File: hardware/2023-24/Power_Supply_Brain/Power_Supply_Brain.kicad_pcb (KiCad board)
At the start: 4 copper layers, 59 x 84 mm, 99 parts, among them J1 Conn_02x03_Odd_Even, J2 Conn_02x02_Counter_Clockwise, J3 USB_B_Micro, J4 Conn_01x02, J5 Screw_Terminal_01x06, J6 Conn_02x11_Counter_Clockwise, SW1 SW_MEC_5G, U1 MAX17502G, U2 RP2040, U3 NCP1117-3.3_SOT223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

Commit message: design updated post review
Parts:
- removed C24: 24n, Capacitor_SMD:C_0805_2012Metric
- removed R29: 120, Resistor_SMD:R_0603_1608Metric
- removed R30: 3.12k, Resistor_SMD:R_0603_1608Metric
- added C30: 12p, Capacitor_SMD:C_0402_1005Metric, F.Cu at (148.8, 65.5)
- added C31: 2200p, Capacitor_SMD:C_0402_1005Metric, F.Cu at (147.6, 66.9)
- added C32: 22p, Capacitor_SMD:C_0402_1005Metric, F.Cu at (133.5, 93.7)
- added C33: 22u, Capacitor_SMD:C_0805_2012Metric, F.Cu at (128.7, 97.5)
- added R21: 20k, Resistor_SMD:R_0402_1005Metric, F.Cu at (149.2, 67.3)
- added R32: 62k, Resistor_SMD:R_0402_1005Metric, F.Cu at (135.3, 91.0)
- added R33: 30k, Resistor_SMD:R_0402_1005Metric, F.Cu at (135.3, 93.7)
- added R34: 135k, Resistor_SMD:R_0402_1005Metric, F.Cu at (132.3, 93.7)
- added R35: 30k, Resistor_SMD:R_0402_1005Metric, F.Cu at (132.3, 91.0)
- C12: value 2.2u -> 10u
- C16: value 910p -> 6800p
- C18: value 10u -> 100n; footprint Capacitor_SMD:C_0805_2012Metric -> Capacitor_SMD:C_0402_1005Metric
- C20, C21: value 27p -> 15p
- L1: value 39u -> 47u
- R13: value 100k -> 174k
- R16: value 11.1k -> 14k
- R4, R5: value 27 -> 27.4
- U3: value NCP1117-3.3_SOT223 -> TPSM861252RDXR; footprint Package_TO_SOT_SMD:SOT-223-3_TabPin2 -> TPSM861252:RDX0007A-MFG
- U5: value NCP1117-ADJ_SOT223 -> NCP1117-5.0_SOT223
- moved C18 9.26 mm to (128.9, 89.2), turned to 180 degrees
- moved C17 4.21 mm to (128.7, 87.2)
- moved U3 2.60 mm to (128.4, 93.1), turned to -90 degrees
- moved C15 1.30 mm to (132.9, 84.2)
- moved R18 0.85 mm to (122.8, 88.4), turned to 90 degrees
- moved C16 0.78 mm to (150.0, 65.5)
- moved C5 0.70 mm to (147.2, 117.3)
- moved U5 0.10 mm to (153.0, 92.1)
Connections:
- net +5.5V renamed +5V
- net /+9V_LX renamed /+12V_LX
- C18 pad 1: +3V3 -> +9V
- U1 pad 7: unconnected-(U1-NC/COMP-Pad7) -> Net-(U1-NC/COMP)
- U2 pad 11: PGD_B2 -> EN_B3
- U2 pad 12: EN_B2 -> PGD_B2
- U2 pad 13: PGD_B1 -> EN_B2
- U2 pad 14: EN_B1 -> PGD_B1
- U2 pad 15: ALRT_B1 -> EN_B1
- U2 pad 16: ALRT_B2 -> ALRT_B1
- U2 pad 17: ALRT_B3 -> ALRT_B2
- U2 pad 18: unconnected-(U2-GPIO15-Pad18) -> ALRT_B3
- U2 pad 8: PGD_B3 -> LED_EN
- U2 pad 9: EN_B3 -> PGD_B3
- U3 pad 1: GND -> +9V
- U3 pad 2: +3V3 -> unconnected-(U3-SW-Pad2)
- U3 pad 3: +9V -> +3V3
- U5 pad 1: Net-(U5-ADJ) -> GND
- U6 pad 1: +3V3 -> LED_EN
- Y1 pad 2: Net-(C21-Pad1) -> GND
- Y1 pad 3: (no net) -> Net-(C21-Pad1)
- Y1 pad 4: (no net) -> GND
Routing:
- net LED_EN: track 0.00 -> 14.4 mm, vias 0 -> 2
- net Net-(U5-ADJ): track 8.00 -> 0.00 mm
- net Net-(U3-EN): track 0.00 -> 7.04 mm, vias 0 -> 2
- net Net-(U3-FB): track 0.00 -> 4.84 mm
- net GND: track 78.4 -> 82.0 mm, vias 58 -> 57
- net EN_B3: track 35.2 -> 32.1 mm
- net +5V: track 33.4 -> 30.4 mm
- net Net-(U1-NC/COMP): track 0.00 -> 2.87 mm
- net +3V3: track 255.8 -> 258.2 mm, vias 29 -> 19
- net Net-(C21-Pad1): track 7.20 -> 5.50 mm
- net PGD_B3: track 36.6 -> 35.4 mm
- net Net-(U2-RUN): track 59.7 -> 58.5 mm
- net Net-(C31-Pad1): track 0.00 -> 1.12 mm
- net +9V: track 27.2 -> 26.5 mm, vias 7 -> 6
- net PGD_B1: track 31.6 -> 30.9 mm
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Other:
- board text added: "9V |5V GND|GND"
- board text removed: "9V |5.5V GND|GND"

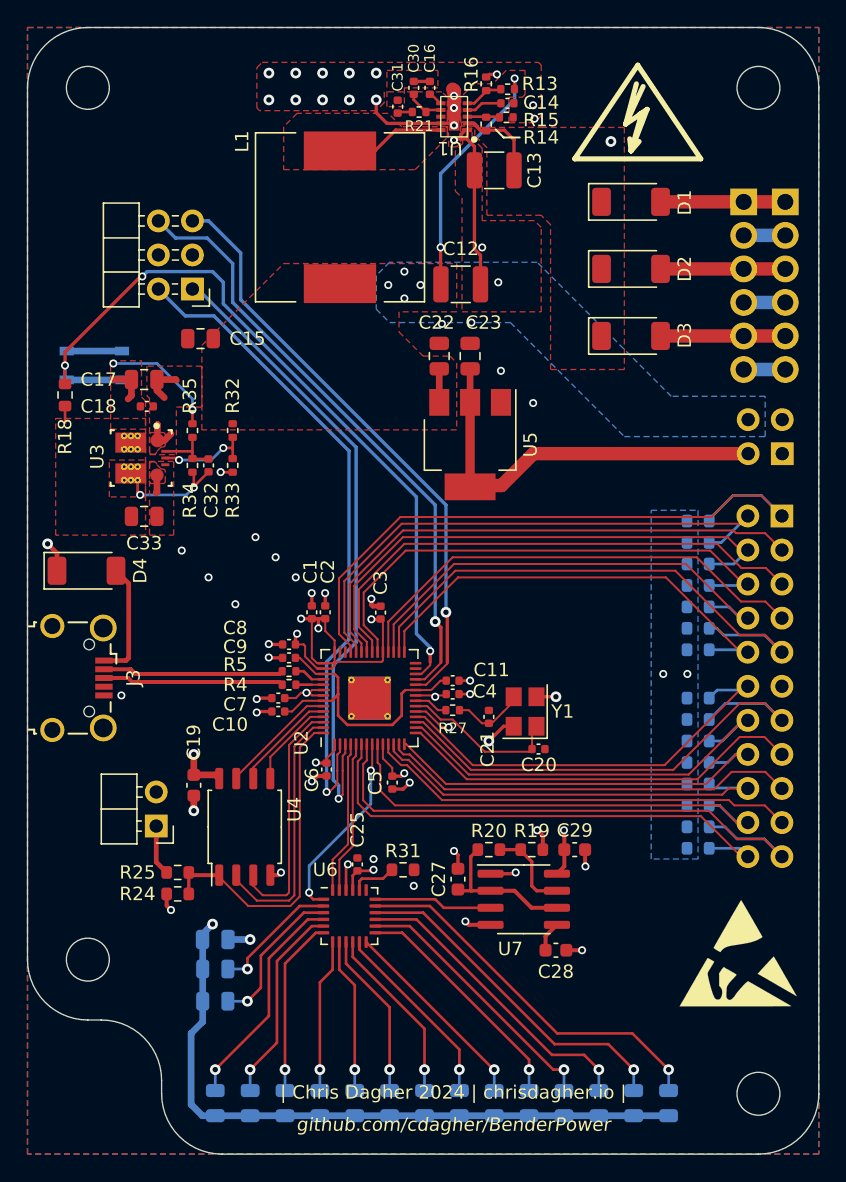
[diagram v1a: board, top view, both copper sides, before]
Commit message: Improved crystal layout. Re-ordered debug connector. Fixed silkscreen.
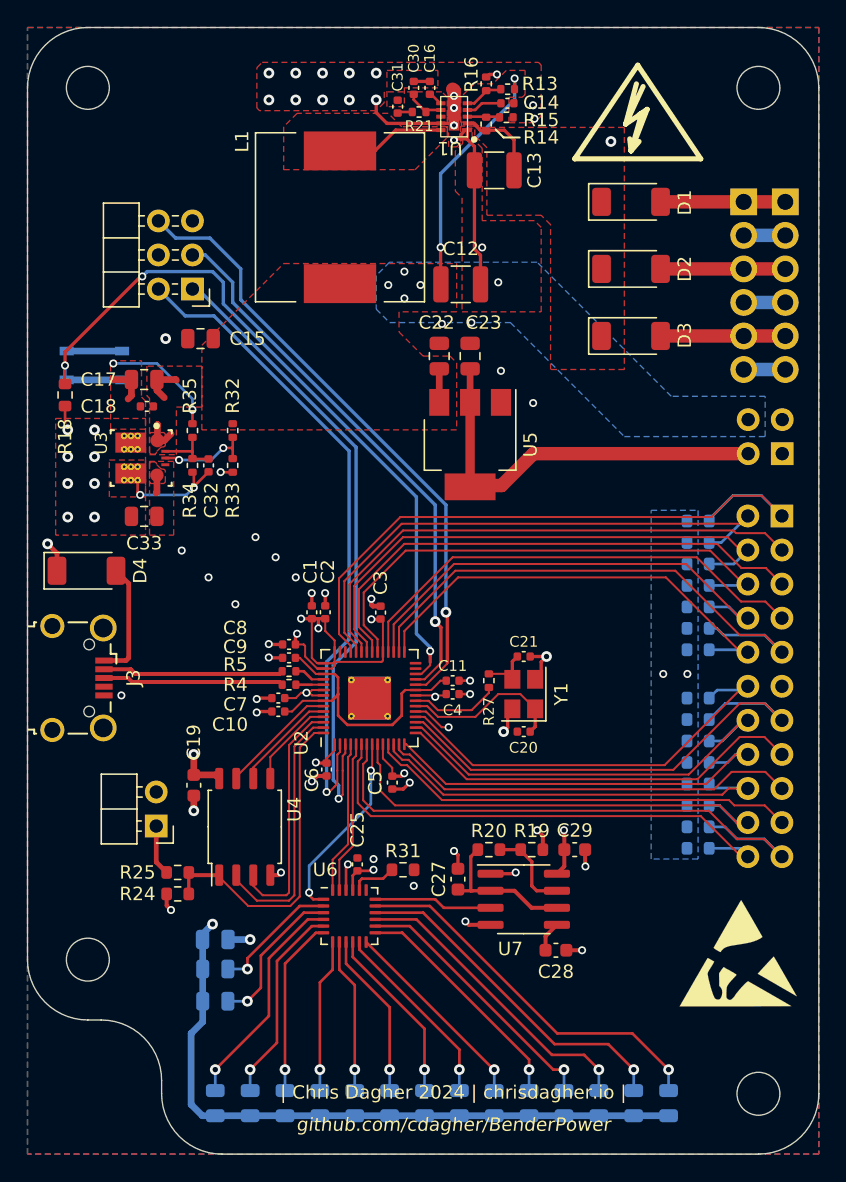
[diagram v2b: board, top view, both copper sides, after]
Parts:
- moved C21 5.20 mm to (157.0, 107.9), turned to 0 degrees
- moved R27 3.48 mm to (154.4, 109.7), turned to 90 degrees
- moved C20 1.70 mm to (157.0, 113.5), turned to 180 degrees
- moved Y1 1.30 mm to (157.0, 110.7)
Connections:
- J1 pad 3: GND -> /SWD
- J1 pad 5: /SWCLK -> GND
- J1 pad 6: /SWD -> /SWCLK
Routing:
- net /SWD: track 45.5 -> 41.0 mm
- net /XOUT: track 2.57 -> 6.69 mm
- net +3V3: track 258.2 -> 260.2 mm, vias 19 -> 27
- net /SWCLK: track 44.6 -> 46.4 mm
- net Net-(C21-Pad1): track 5.50 -> 3.77 mm
- net GND: track 82.0 -> 83.5 mm, vias 57 -> 58
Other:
- board text added: "12V| 5V GND|GND"
- board text added: "CLK GND"
- board text removed: "9V |5V GND|GND"
- board text removed: "GND CLK"

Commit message: Pushing for pre-production review
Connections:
- J6 pad 11: unconnected-(J6-Pin_11-Pad11) -> GND
- U3 pad 11: (no net) -> +3V3
- U3 pad 12: (no net) -> +3V3
- U3 pad 13: (no net) -> +3V3
- U3 pad 17: (no net) -> +3V3
- U3 pad 18: (no net) -> +3V3
- U3 pad 19: (no net) -> +3V3
- U3 pad 2: unconnected-(U3-SW-Pad2) -> (no net)
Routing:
- net GND: track 83.5 -> 92.1 mm
